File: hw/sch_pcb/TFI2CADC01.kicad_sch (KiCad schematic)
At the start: 31 parts, among them J1 SM04B-GHS-TB, J2 SM04B-GHS-TB, J3 SM04B-GHS-TB, J4 SM04B-GHS-TB, J5 SM04B-GHS-TB, J6 SM04B-GHS-TB, U1 MIC5504-3.3YM5, U2 LTC4317

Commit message: Hotové schéma - otázka jumpery a konektory na vstupu
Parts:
- removed J1, J2, J5, J6: SM04B-GHS-TB, Connector_JST:JST_GH_SM04B-GHS-TB_1x04-1MP_P1.25mm_Horizontal, symbol MLAB_CONNECTORS_JST:SM04B-GHS-TB
- removed R10, R12, R15: 1M, Resistor_SMD:R_0603_1608Metric, symbol Device:R
- removed R13, R14, R9: 887k, Resistor_SMD:R_0603_1608Metric, symbol Device:R
- removed R16, R17, R2, R3: 10k, Resistor_SMD:R_0603_1608Metric, symbol Device:R
- removed R7: -, Resistor_SMD:R_0603_1608Metric, symbol Device:R
- removed R8: 180R, Resistor_SMD:R_0603_1608Metric, symbol Device:R
- removed U2: LTC4317, Package_DFN_QFN:DFN-16-1EP_3x5mm_P0.5mm_EP1.66x4.4mm, symbol Interface_Expansion:LTC4317
- added C5: 100nF, Capacitor_SMD:C_0603_1608Metric, symbol Device:C
- added D3: LED RED, LED_SMD:LED_0603_1608Metric, symbol Device:LED
- added J2: ALERT/RDY, TestPoint:TestPoint_Keystone_5015_Micro_Mini, symbol Connector:TestPoint
- added J5: Conn_01x06_Pin, Connector_PinHeader_2.54mm:PinHeader_1x06_P2.54mm_Horizontal, symbol Connector:Conn_01x06_Pin
- added JP3: 0x4A, Jumper:SolderJumper-2_P1.3mm_Open_RoundedPad1.0x1.5mm, symbol Jumper:SolderJumper_2_Open
- added JP4: 0x4B, Jumper:SolderJumper-2_P1.3mm_Open_RoundedPad1.0x1.5mm, symbol Jumper:SolderJumper_2_Open
- added JP5: Jumper_3_Bridged12, Jumper:SolderJumper-3_P1.3mm_Bridged12_Pad1.0x1.5mm_NumberLabels, symbol Jumper:Jumper_3_Bridged12
- added Q1: BC817, Package_TO_SOT_SMD:SOT-23, symbol Transistor_BJT:BC817
- added R4, R5: 10k, Resistor_SMD:R_0603_1608Metric, symbol Device:R
- added R6: 180R, Resistor_SMD:R_0603_1608Metric, symbol Device:R
- added U3: ADS1115IDGS, Package_SO:TSSOP-10_3x3mm_P0.5mm, symbol Analog_ADC:ADS1115IDGS
- C4: value 100nF -> 10uF
- JP1: value SolderJumper_2_Open -> 0x48
- JP2: value SolderJumper_2_Open -> 0x49
- renumbered R5 to R2, R6 to R3
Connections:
- net XORL2 is gone; now on net ADDR: JP2.1 (A)
- net +3V3: now also C5.1, J5.6 (Pin_6), JP5.2 (C), R4.1, U3.8 (VDD); no longer JP1.2 (B)
- net +5V: now also R6.1
- net GND: now also JP1.2 (B), C5.2, J5.1 (Pin_1), JP5.3 (B), Q1.2 (E), U3.3 (GND)
- net SCLout1 renamed SCL
- net SCL: now also JP4.2 (B), U3.10 (SCL)
- net SDAout1 renamed SDA
- net SDA: now also JP3.2 (B), U3.9 (SDA)
- net XORL1 renamed ADDR
- net ADDR: now also JP3.1 (A), JP4.1 (A), JP5.1 (A), U3.1 (ADDR)
- new net: D3.2 (A), R6.2
- new net: D3.1 (K), Q1.3 (C)
- new net: Q1.1 (B), R5.1
- new net AIN0: J5.5 (Pin_5), U3.4 (AIN0)
- new net AIN1: J5.4 (Pin_4), U3.5 (AIN1)
- new net AIN2: J5.3 (Pin_3), U3.6 (AIN2)
- new net AIN3: J5.2 (Pin_2), U3.7 (AIN3)
- new net ALERT/RDY: J2.1, R4.2, R5.2, U3.2 (ALERT/RDY)
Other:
- note added: "0x48"
- note added: "0x49"
- note added: "I2C ADDRESS JUMPER"
- note removed: "Address XOR translations: Output 1 (JP1): Open - 0x08 Shorted - 0x0f Output 2 (JP2): Open - 0x78 Shorted - 0x7f"
- moved on the sheet: C1, C2, C3, D1, D2, J3, J4, R1, R2, R3, U1

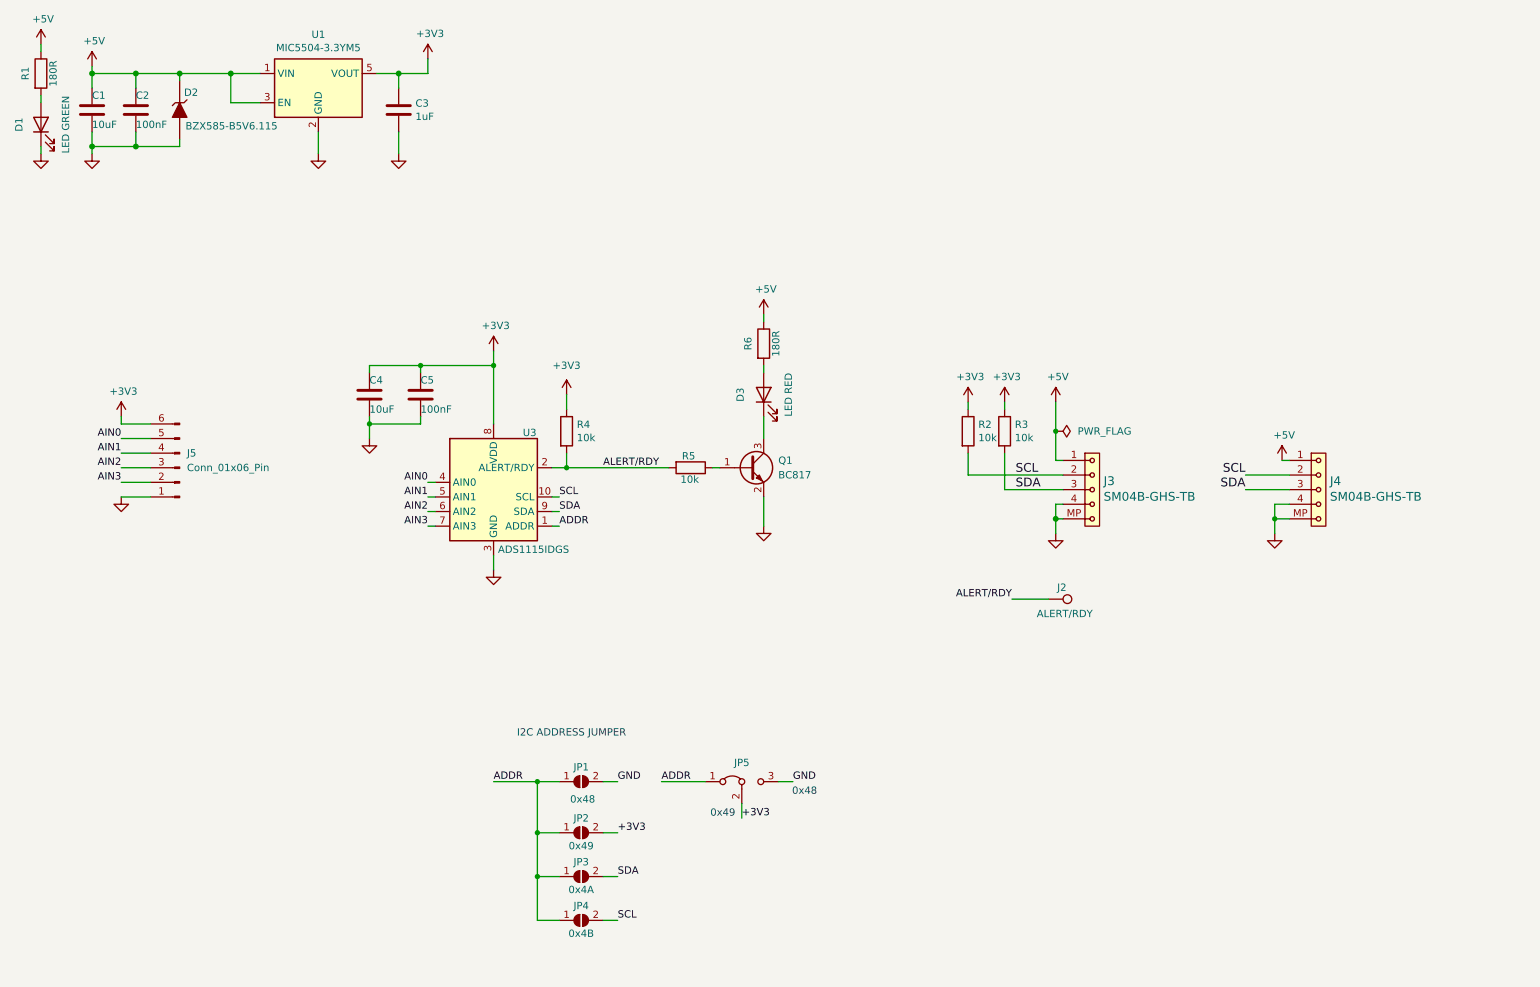
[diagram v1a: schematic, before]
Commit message: ADS1115 obvod s headry
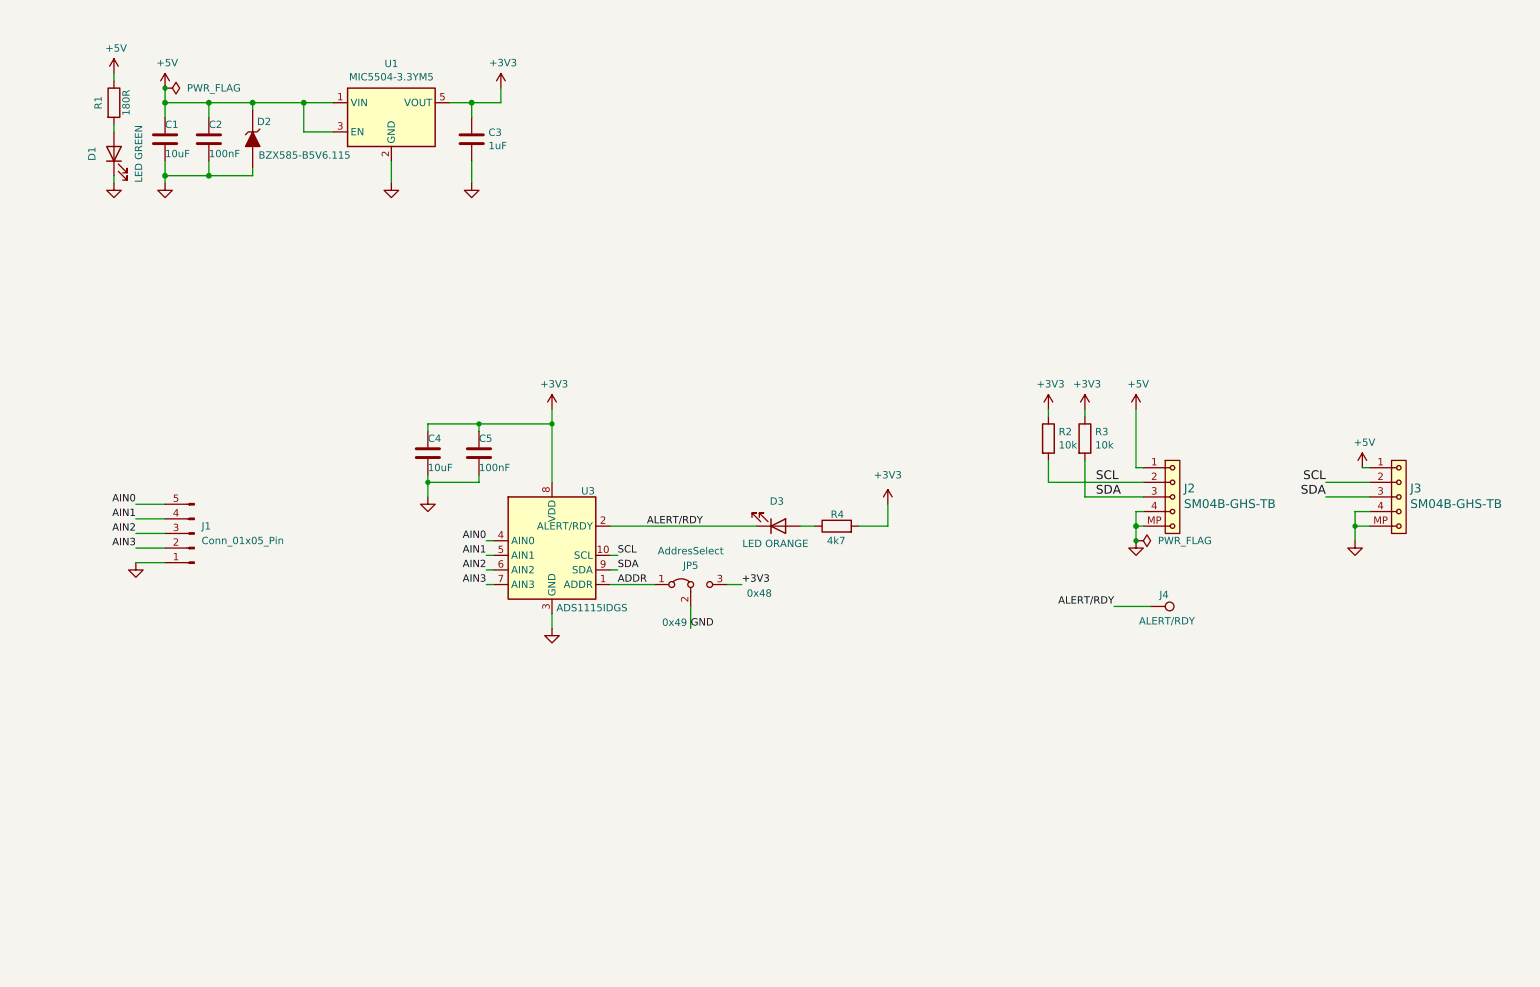
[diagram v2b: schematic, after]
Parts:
- removed J5: Conn_01x06_Pin, Connector_PinHeader_2.54mm:PinHeader_1x06_P2.54mm_Horizontal, symbol Connector:Conn_01x06_Pin
- removed JP1: 0x48, Jumper:SolderJumper-2_P1.3mm_Open_RoundedPad1.0x1.5mm, symbol Jumper:SolderJumper_2_Open
- removed JP2: 0x49, Jumper:SolderJumper-2_P1.3mm_Open_RoundedPad1.0x1.5mm, symbol Jumper:SolderJumper_2_Open
- removed JP3: 0x4A, Jumper:SolderJumper-2_P1.3mm_Open_RoundedPad1.0x1.5mm, symbol Jumper:SolderJumper_2_Open
- removed JP4: 0x4B, Jumper:SolderJumper-2_P1.3mm_Open_RoundedPad1.0x1.5mm, symbol Jumper:SolderJumper_2_Open
- removed Q1: BC817, Package_TO_SOT_SMD:SOT-23, symbol Transistor_BJT:BC817
- removed R5: 10k, Resistor_SMD:R_0603_1608Metric, symbol Device:R
- removed R6: 180R, Resistor_SMD:R_0603_1608Metric, symbol Device:R
- added J1: Conn_01x05_Pin, Connector_PinHeader_2.54mm:PinHeader_1x05_P2.54mm_Horizontal, symbol Connector:Conn_01x05_Pin
- C1: footprint Capacitor_SMD:C_0805_2012Metric -> Mlab_R:SMD-0603
- C2, C3, C4, C5: footprint Capacitor_SMD:C_0603_1608Metric -> Mlab_R:SMD-0603
- D1: footprint LED_SMD:LED_0603_1608Metric -> Mlab_D:LED_1206_mill
- D3: value LED RED -> LED ORANGE; footprint LED_SMD:LED_0603_1608Metric -> Mlab_D:LED_1206_mill
- JP5: value Jumper_3_Bridged12 -> AddresSelect
- R2, R3: footprint Resistor_SMD:R_0603_1608Metric -> Mlab_R:SMD-0603
- R4: value 10k -> 4k7; footprint Resistor_SMD:R_0603_1608Metric -> Mlab_R:SMD-0603
- renumbered J3 to J2, J4 to J3, J2 to J4
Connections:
- net +3V3: now also JP5.3 (B), R4.2; no longer JP5.2 (C), R4.1
- net AIN0: now also J1.5 (Pin_5)
- net AIN1: now also J1.4 (Pin_4)
- net AIN2: now also J1.3 (Pin_3)
- net AIN3: now also J1.2 (Pin_2)
- net ALERT/RDY: now also D3.1 (K); no longer R4.2
- net GND: now also JP5.2 (C), J1.1 (Pin_1); no longer JP5.3 (B)
- net at D3.2 (A): now also R4.1
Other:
- note removed: "I2C ADDRESS JUMPER"
- moved on the sheet: C1, C2, C3, C4, C5, D1, D2, J2, J3, J4, JP5, R1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

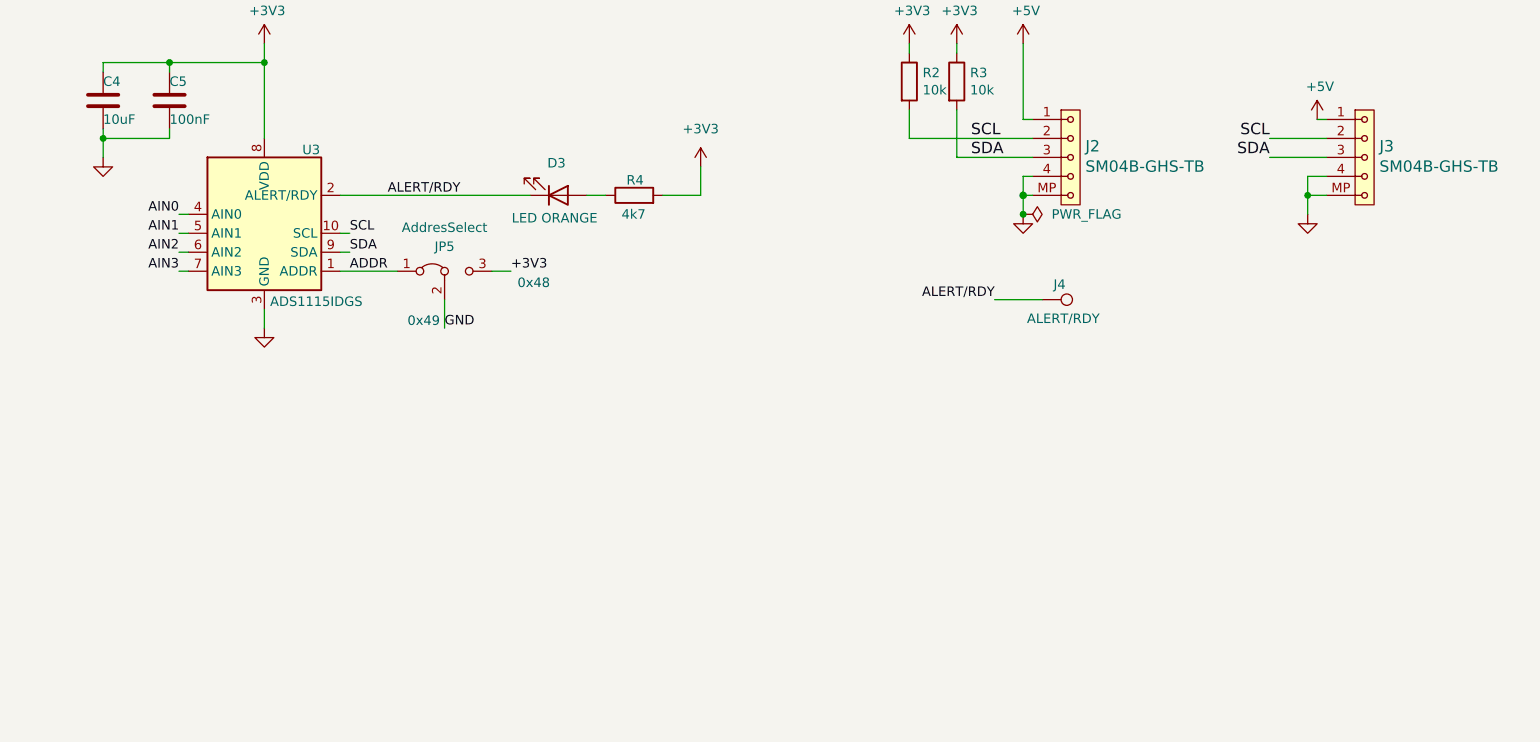
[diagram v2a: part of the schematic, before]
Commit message: Adding address selection
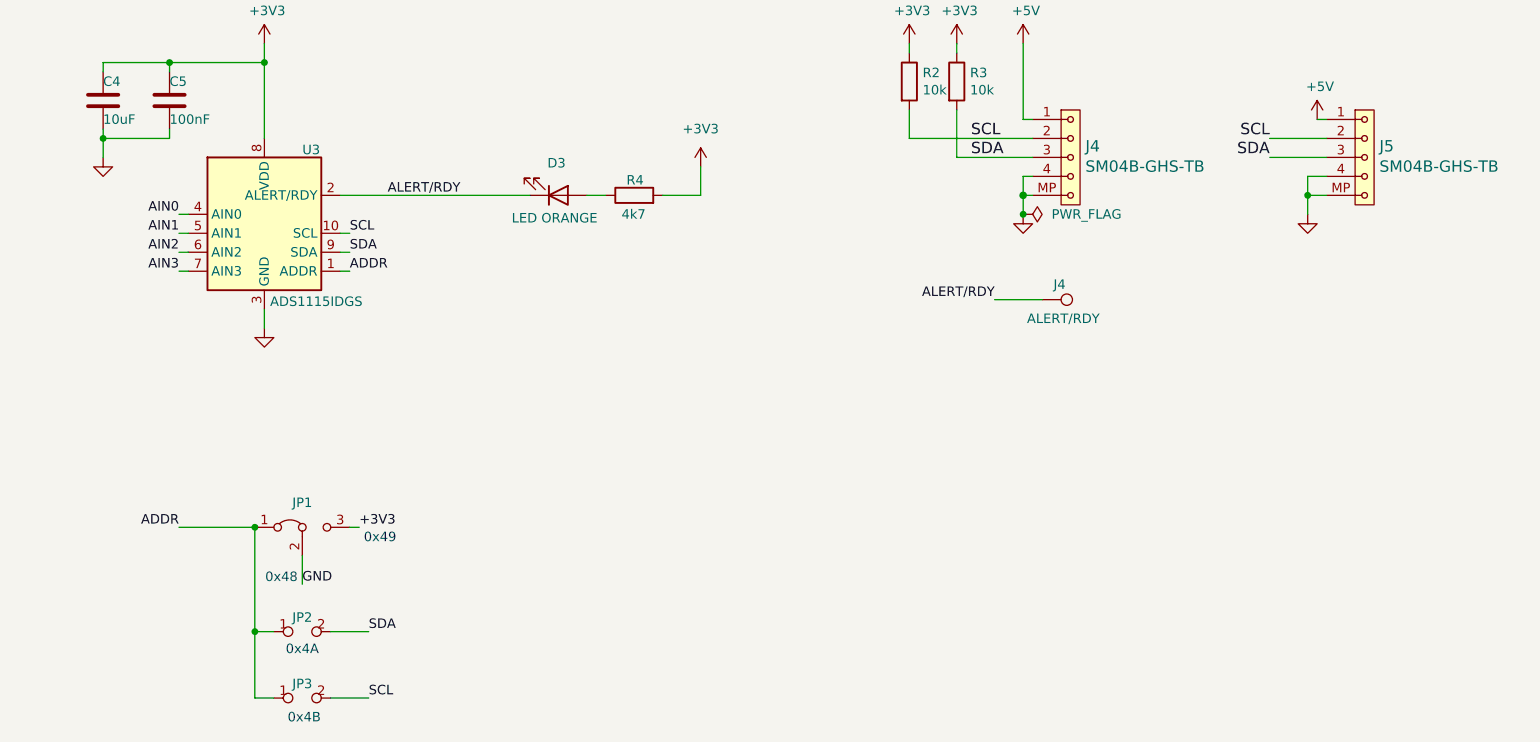
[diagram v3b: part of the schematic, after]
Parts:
- added JP2: 0x4A, Jumper:SolderJumper-2_P1.3mm_Open_TrianglePad1.0x1.5mm, symbol e-radionica.com schematics:SMD_JUMPER
- added JP3: 0x4B, Jumper:SolderJumper-2_P1.3mm_Open_TrianglePad1.0x1.5mm, symbol e-radionica.com schematics:SMD_JUMPER
- renumbered J2 to J4, J3 to J5, JP5 to JP1
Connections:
- net ADDR: now also JP2.1, JP3.1
- net SCL: now also JP3.2
- net SDA: now also JP2.2
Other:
- note added: "0x4A"
- note added: "0x4B"
- moved on the sheet: JP1
